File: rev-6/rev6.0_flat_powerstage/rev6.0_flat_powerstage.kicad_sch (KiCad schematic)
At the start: 266 parts, among them J1 PHASE_SIG, J2 ENC_SIG, J3 POWER, J5 ANALOG_SIG, J6 VBUS, J7 Motor, Q1 LMG5200, Q2 LMG5200, Q3 LMG5200, U1 AS5047D, U10 LT6350, U11 LP5900SD-3.3/NOPB, U12 LM4040C30FTA, U13 MA730, U2 INA240A1PW, U3 LT6350, U4 TLV76750DRVR, U5 INA240A1PW, U6 LT6350, U7 NCP115ASN330T2G, U8 LT6350, U9 INA240A1PW

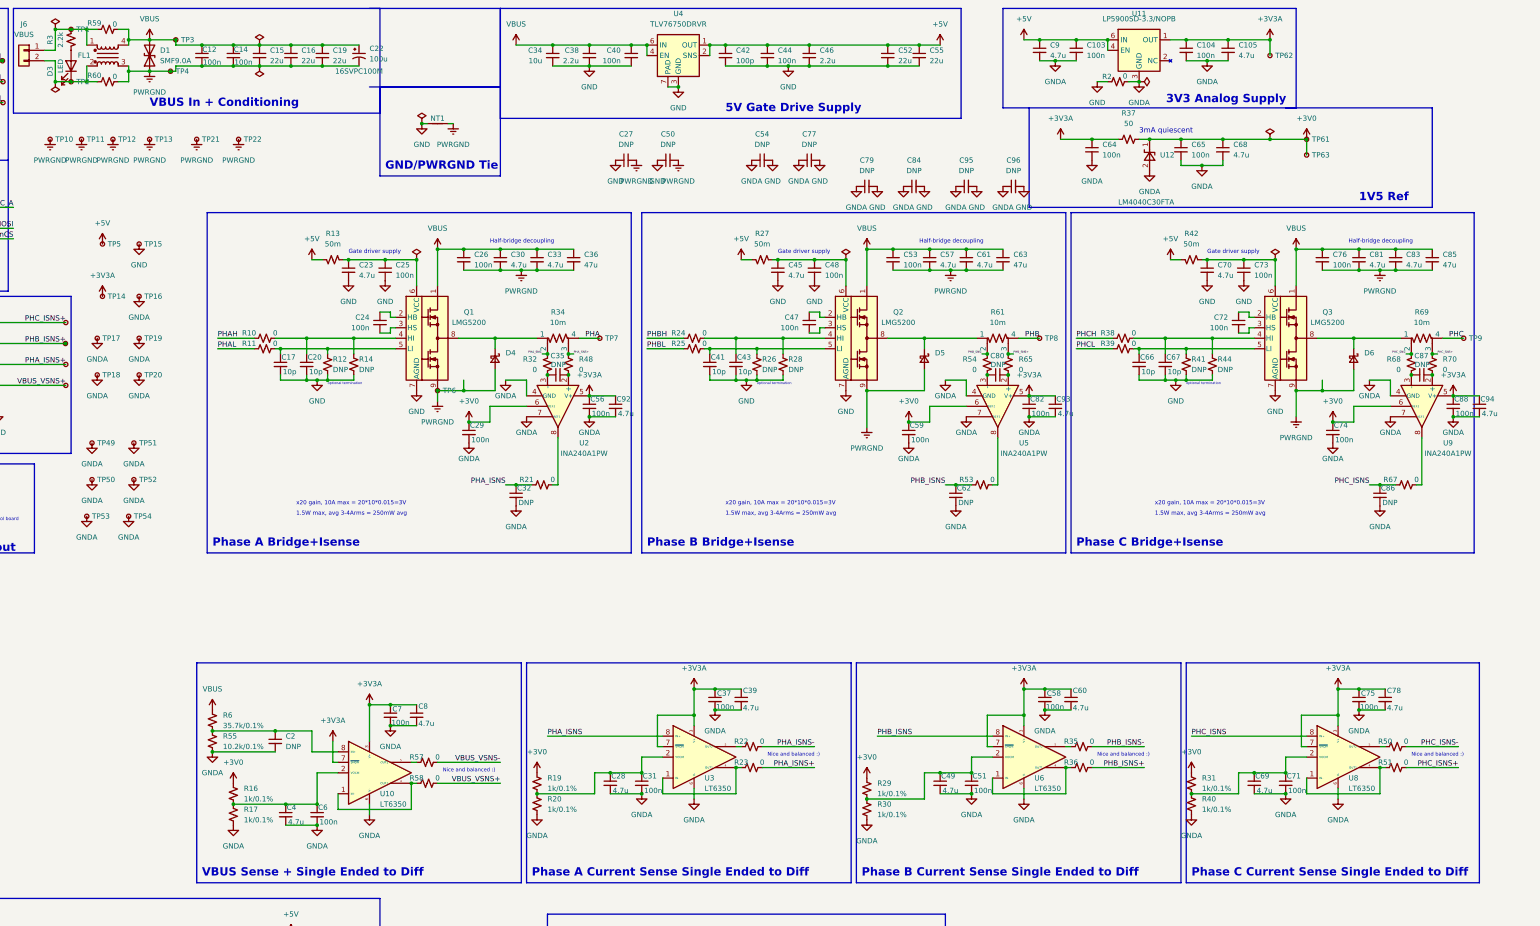
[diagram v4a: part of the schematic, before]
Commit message: Add nonsplit ground version
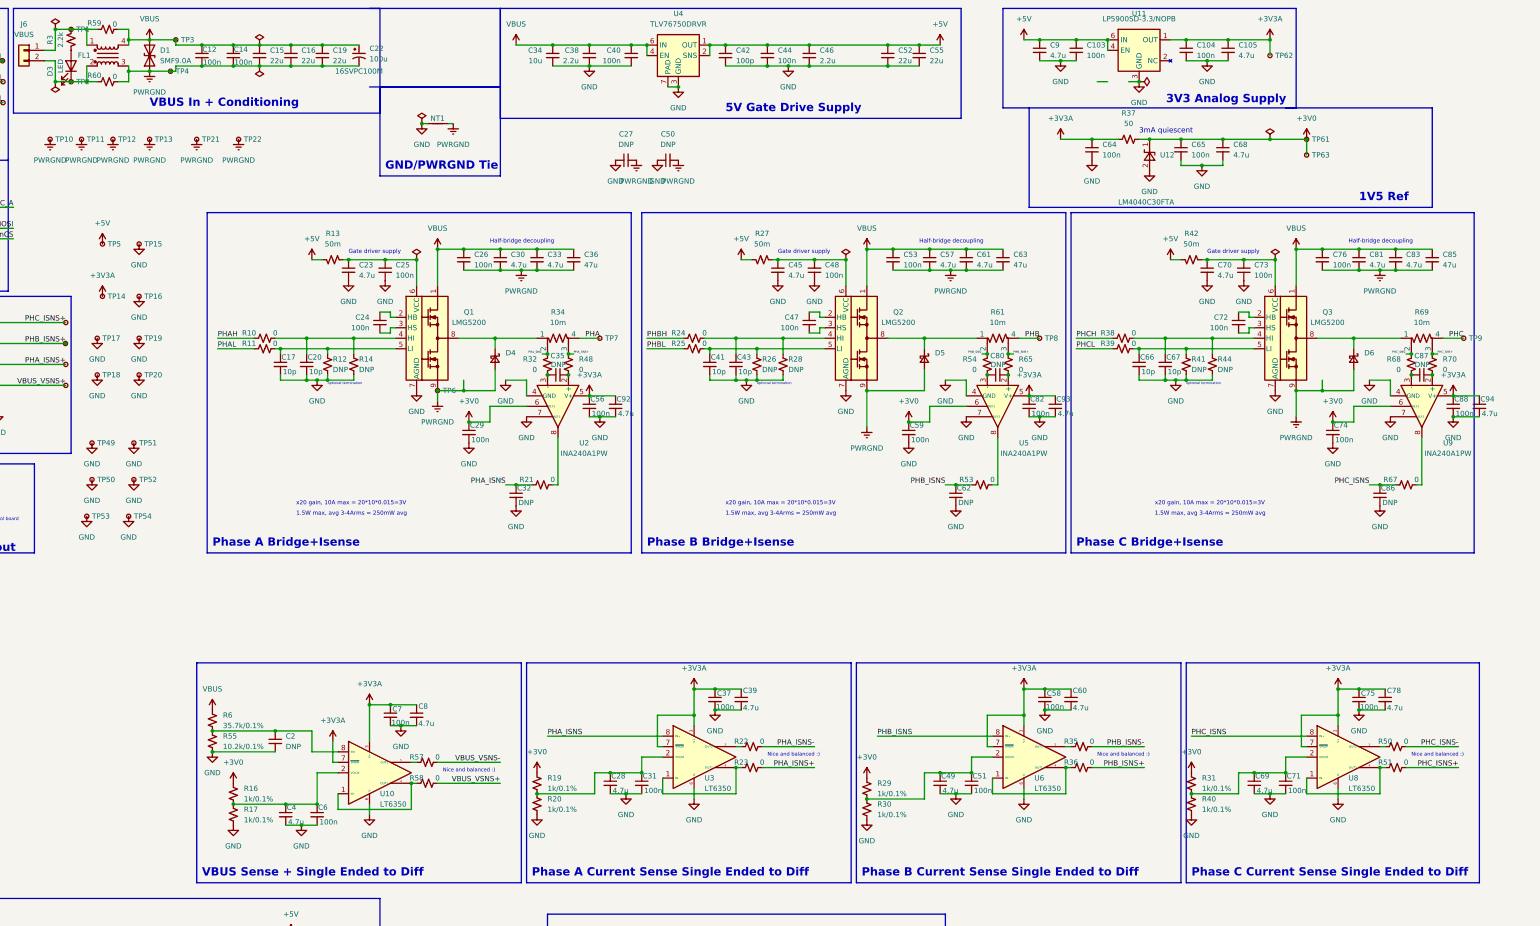
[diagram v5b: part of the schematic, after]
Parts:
- removed C54, C77, C79, C84, C95, C96: DNP, Capacitor_SMD:C_0603_1608Metric, symbol Device:C_Small
- removed R2: 0, Resistor_SMD:R_0603_1608Metric, symbol Device:R_Small_US
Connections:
- net GNDA is gone; now on net GND: C103.2, C104.2, C105.2, C2.2, C28.2, C29.2, C31.2, C32.2, C37.2, C39.2, C4.2, C49.2, C51.2, C56.2, C58.2, C59.2, C6.2, C60.2, C62.2, C64.2, C65.2, C68.2, C69.2, C7.2, C71.2, C74.2, C75.2, C78.2, C8.2, C82.2, C86.2, C88.2, C9.2, C92.2, C93.2, C94.2, R17.1, R20.1, R30.1, R40.1, R55.2, TP16.1, TP17.1, TP18.1, TP19.1, TP20.1, TP49.1, TP50.1, TP51.1, TP52.1, TP53.1, TP54.1, U10.6 (V-), U10.9 (EP), U11.3 (GND), U11.7 (GND), U12.2 (A), U2.1 (GND), U2.4 (GND), U2.7 (REF1), U3.6 (V-), U3.9 (EP), U5.1 (GND), U5.4 (GND), U5.7 (REF1), U6.6 (V-), U6.9 (EP), U8.6 (V-), U8.9 (EP), U9.1 (GND), U9.4 (GND), U9.7 (REF1)
